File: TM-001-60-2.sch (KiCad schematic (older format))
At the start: 14 parts

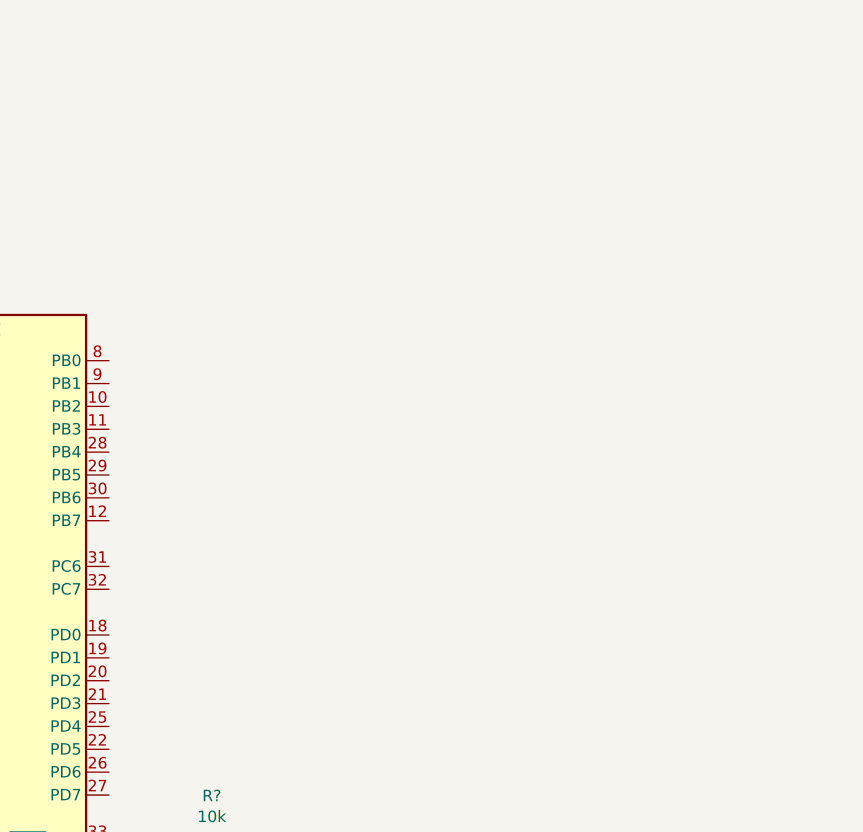
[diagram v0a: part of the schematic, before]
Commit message: Complete rest of schematic
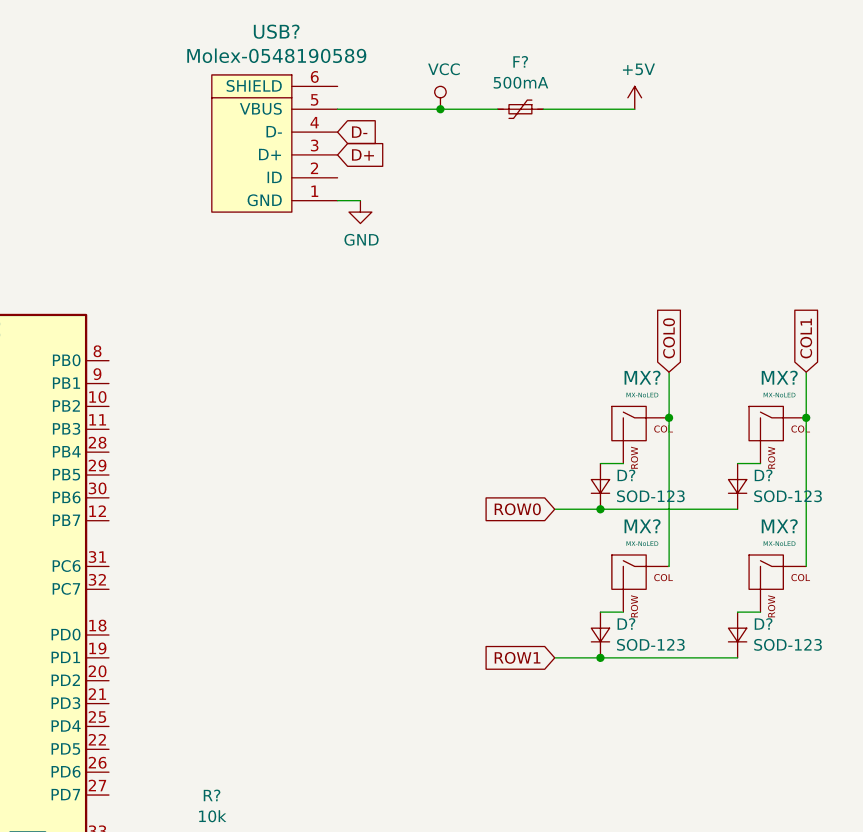
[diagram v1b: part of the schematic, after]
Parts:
- added D? (x4): SOD-123, symbol Device:D_Small
- added F?: 500mA, symbol Device:Polyfuse_Small
- added MX? (x4): MX-NoLED, symbol MX_Alps_Hybrid:MX-NoLED
- added USB?: Molex-0548190589, symbol random-keyboard-parts:Molex-0548190589
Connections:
- net +5V: now also F?.1
- net D+: now also USB?.3 (D+)
- net D-: now also USB?.4 (D-)
- net GND: now also USB?.1 (GND)
- new net: D?.2 (A), MX?.2 (ROW) (x4)
- new net COL0: MX?.1 (COL), MX?.1 (COL)
- new net COL1: MX?.1 (COL), MX?.1 (COL)
- new net ROW0: D?.1 (K), D?.1 (K)
- new net ROW1: D?.1 (K), D?.1 (K)
- new net VCC: F?.2, USB?.5 (VBUS)
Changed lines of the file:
@@
 EESchema Schematic File Version 4
+LIBS:TM-001-60-2-cache
 EELAYER 30 0
 EELAYER END
@@
 Text GLabel 1500 3600 0    50   Input ~ 0
 D-
+$Comp
+L Device:Polyfuse_Small F?
+U 1 1 6201AF9A
+P 6050 1400
+F 0 "F?" V 5845 1400 50  0000 C CNN
+F 1 "500mA" V 5936 1400 50  0000 C CNN
+F 2 "" H 6100 1200 50  0001 L CNN
+F 3 "~" H 6050 1400 50  0001 C CNN
+	1    6050 1400
+	0    1    1    0
+$EndComp
+$Comp
+L random-keyboard-parts:Molex-0548190589 USB?
+U 1 1 62018580
+P 4950 1600
+F 0 "USB?" V 5487 1567 60  0000 C CNN
+F 1 "Molex-0548190589" V 5381 1567 60  0000 C CNN
+F 2 "" H 4950 1600 60  0001 C CNN
+F 3 "" H 4950 1600 60  0001 C CNN
+	1    4950 1600
+	0    -1   -1   0
+$EndComp
+$Comp
+L power:VCC #PWR?
+U 1 1 6201E04C
+P 5700 1400
+F 0 "#PWR?" H 5700 1250 50  0001 C CNN
+F 1 "VCC" H 5717 1573 50  0000 C CNN
+F 2 "" H 5700 1400 50  0001 C CNN
+F 3 "" H 5700 1400 50  0001 C CNN
+	1    5700 1400
+	1    0    0    -1
+$EndComp
+Wire Wire Line
+	5250 1400 5700 1400
+Wire Wire Line
+	5950 1400 5700 1400
+Connection ~ 5700 1400
+$Comp
+L power:+5V #PWR?
+U 1 1 62020679
+P 6550 1400
+F 0 "#PWR?" H 6550 1250 50  0001 C CNN
+F 1 "+5V" H 6565 1573 50  0000 C CNN
+F 2 "" H 6550 1400 50  0001 C CNN
+F 3 "" H 6550 1400 50  0001 C CNN
+	1    6550 1400
+	1    0    0    -1
+$EndComp
+Wire Wire Line
+	6150 1400 6550 1400
+Text GLabel 5250 1500 2    50   Input ~ 0
+D-
+Text GLabel 5250 1600 2    50   Input ~ 0
+D+
+$Comp
+L power:GND #PWR?
+U 1 1 62022B0D
+P 5350 1800
+F 0 "#PWR?" H 5350 1550 50  0001 C CNN
+F 1 "GND" H 5355 1627 50  0000 C CNN
+F 2 "" H 5350 1800 50  0001 C CNN
+F 3 "" H 5350 1800 50  0001 C CNN
+	1    5350 1800
+	1    0    0    -1
+$EndComp
+Wire Wire Line
+	5250 1800 5350 1800
+$Comp
+L MX_Alps_Hybrid:MX-NoLED MX?
+U 1 1 62024221
+P 6550 2800
+F 0 "MX?" H 6583 3023 60  0000 C CNN
+F 1 "MX-NoLED" H 6583 2949 20  0000 C CNN
+F 2 "" H 5925 2775 60  0001 C CNN
+F 3 "" H 5925 2775 60  0001 C CNN
+	1    6550 2800
+	1    0    0    -1
+$EndComp
+$Comp
+L Device:D_Small D?
+U 1 1 62024CA8
+P 6400 3050
+F 0 "D?" V 6446 2982 50  0000 R CNN
+F 1 "SOD-123" V 6355 2982 50  0000 R CNN
+F 2 "" V 6400 3050 50  0001 C CNN
+F 3 "~" V 6400 3050 50  0001 C CNN
+	1    6400 3050
+	0    -1   -1   0
+$EndComp
+Wire Wire Line
+	6400 2950 6500 2950
+$Comp
+L MX_Alps_Hybrid:MX-NoLED MX?
+U 1 1 6202664B
+P 7150 2800
+F 0 "MX?" H 7183 3023 60  0000 C CNN
+F 1 "MX-NoLED" H 7183 2949 20  0000 C CNN
+F 2 "" H 6525 2775 60  0001 C CNN
+F 3 "" H 6525 2775 60  0001 C CNN
+	1    7150 2800
+	1    0    0    -1
+$EndComp
+$Comp
+L Device:D_Small D?
+U 1 1 62027277
+P 7000 3050
+F 0 "D?" V 7046 2982 50  0000 R CNN
+F 1 "SOD-123" V 6955 2982 50  0000 R CNN
+F 2 "" V 7000 3050 50  0001 C CNN
+F 3 "~" V 7000 3050 50  0001 C CNN
+	1    7000 3050
+	0    -1   -1   0
+$EndComp
+Wire Wire Line
+	7000 2950 7100 2950
+$Comp
+L MX_Alps_Hybrid:MX-NoLED MX?
+U 1 1 6202C76A
+P 6550 3450
+F 0 "MX?" H 6583 3673 60  0000 C CNN
+F 1 "MX-NoLED" H 6583 3599 20  0000 C CNN
+F 2 "" H 5925 3425 60  0001 C CNN
+F 3 "" H 5925 3425 60  0001 C CNN
+	1    6550 3450
+	1    0    0    -1
+$EndComp
+$Comp
+L Device:D_Small D?
+U 1 1 6202CF72
+P 6400 3700
+F 0 "D?" V 6446 3632 50  0000 R CNN
+F 1 "SOD-123" V 6355 3632 50  0000 R CNN
+F 2 "" V 6400 3700 50  0001 C CNN
+F 3 "~" V 6400 3700 50  0001 C CNN
+	1    6400 3700
+	0    -1   -1   0
+$EndComp
+Wire Wire Line
+	6400 3600 6500 3600
+$Comp
+L MX_Alps_Hybrid:MX-NoLED MX?
+U 1 1 6202E4F6
+P 7150 3450
+F 0 "MX?" H 7183 3673 60  0000 C CNN
+F 1 "MX-NoLED" H 7183 3599 20  0000 C CNN
+F 2 "" H 6525 3425 60  0001 C CNN
+F 3 "" H 6525 3425 60  0001 C CNN
+	1    7150 3450
+	1    0    0    -1
+$EndComp
+$Comp
+L Device:D_Small D?
+U 1 1 6202F015
+P 7000 3700
+F 0 "D?" V 7046 3632 50  0000 R CNN
+F 1 "SOD-123" V 6955 3632 50  0000 R CNN
+F 2 "" V 7000 3700 50  0001 C CNN
+F 3 "~" V 7000 3700 50  0001 C CNN
+	1    7000 3700
+	0    -1   -1   0
+$EndComp
+Wire Wire Line
+	7000 3600 7100 3600
+Wire Wire Line
+	6700 3400 6700 2750
+Connection ~ 6700 2750
+Wire Wire Line
+	6700 2750 6700 2550
+Wire Wire Line
+	7300 3400 7300 2750
+Connection ~ 7300 2750
+Wire Wire Line
+	7300 2750 7300 2550
+Wire Wire Line
+	7000 3150 6400 3150
+Connection ~ 6400 3150
+Wire Wire Line
+	6400 3150 6200 3150
+Wire Wire Line
+	7000 3800 6400 3800
+Connection ~ 6400 3800
+Wire Wire Line
+	6400 3800 6200 3800
+Text GLabel 6200 3150 0    50   Input ~ 0
+ROW0
+Text GLabel 6200 3800 0    50   Input ~ 0
+ROW1
+Text GLabel 6700 2550 1    50   Input ~ 0
+COL0
+Text GLabel 7300 2550 1    50   Input ~ 0
+COL1
 $EndSCHEMATC

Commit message: ready to create pcb
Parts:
- C1, C2, C3, C4, C5, C6, C7: renamed from C?; footprint (none) -> Capacitor_SMD:C_0805_2012Metric
- D1, D2, D3, D4: renamed from D?; footprint (none) -> Diode_SMD:D_SOD-123
- F1: renamed from F?; footprint (none) -> Fuse:Fuse_1206_3216Metric
- MX1, MX2, MX3, MX4: renamed from MX?; footprint (none) -> MX_Alps_Hybrid:MX-1U-NoLED
- SW1: renamed from SW?; footprint (none) -> random-keyboard-parts:SKQG-1155865
- USB1: renamed from USB?; footprint (none) -> random-keyboard-parts:Molex-0548190589
- Y1: renamed from Y?; footprint (none) -> Crystal:Crystal_SMD_3225-4Pin_3.2x2.5mm
- gave numbers to parts that had none: 5

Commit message: fixed footprint assigning
i forgor resistors
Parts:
- R1, R2, R3, R4: footprint (none) -> Resistor_SMD:R_0805_2012Metric
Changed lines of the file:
@@
 F 0 "R4" V 4504 4600 50  0000 C CNN
 F 1 "10k" V 4595 4600 50  0000 C CNN
-F 2 "" H 4700 4600 50  0001 C CNN
+F 2 "Resistor_SMD:R_0805_2012Metric" H 4700 4600 50  0001 C CNN
 F 3 "~" H 4700 4600 50  0001 C CNN
 	1    4700 4600
@@
 F 0 "R2" V 2104 3500 50  0000 C CNN
 F 1 "22" V 2195 3500 50  0000 C CNN
-F 2 "" H 2300 3500 50  0001 C CNN
+F 2 "Resistor_SMD:R_0805_2012Metric" H 2300 3500 50  0001 C CNN
 F 3 "~" H 2300 3500 50  0001 C CNN
 	1    2300 3500
@@
 F 0 "R3" V 1604 3600 50  0000 C CNN
 F 1 "22" V 1695 3600 50  0000 C CNN
-F 2 "" H 1800 3600 50  0001 C CNN
+F 2 "Resistor_SMD:R_0805_2012Metric" H 1800 3600 50  0001 C CNN
 F 3 "~" H 1800 3600 50  0001 C CNN
 	1    1800 3600
@@
 F 0 "R1" H 3059 2196 50  0000 L CNN
 F 1 "10k" H 3059 2105 50  0000 L CNN
-F 2 "" H 3000 2150 50  0001 C CNN
+F 2 "Resistor_SMD:R_0805_2012Metric" H 3000 2150 50  0001 C CNN
 F 3 "~" H 3000 2150 50  0001 C CNN
 	1    3000 2150

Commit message: saved schematic
i forgor *insert skull emoji*
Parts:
- MX1, MX2, MX3, MX4: footprint MX_Alps_Hybrid:MX-1U-NoLED -> MX_Alps_Hybrid:MX-1U
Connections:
- net COL0: now also U1.29 (PB5)
- net COL1: now also U1.28 (PB4)
- net ROW0: now also U1.27 (PD7)
- net ROW1: now also U1.30 (PB6)
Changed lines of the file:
@@
 F 0 "MX1" H 6583 3023 60  0000 C CNN
 F 1 "MX-NoLED" H 6583 2949 20  0000 C CNN
-F 2 "MX_Alps_Hybrid:MX-1U-NoLED" H 5925 2775 60  0001 C CNN
+F 2 "MX_Alps_Hybrid:MX-1U" H 5925 2775 60  0001 C CNN
 F 3 "" H 5925 2775 60  0001 C CNN
 	1    6550 2800
@@
 F 0 "MX2" H 7183 3023 60  0000 C CNN
 F 1 "MX-NoLED" H 7183 2949 20  0000 C CNN
-F 2 "MX_Alps_Hybrid:MX-1U-NoLED" H 6525 2775 60  0001 C CNN
+F 2 "MX_Alps_Hybrid:MX-1U" H 6525 2775 60  0001 C CNN
 F 3 "" H 6525 2775 60  0001 C CNN
 	1    7150 2800
@@
 F 0 "MX3" H 6583 3673 60  0000 C CNN
 F 1 "MX-NoLED" H 6583 3599 20  0000 C CNN
-F 2 "MX_Alps_Hybrid:MX-1U-NoLED" H 5925 3425 60  0001 C CNN
+F 2 "MX_Alps_Hybrid:MX-1U" H 5925 3425 60  0001 C CNN
 F 3 "" H 5925 3425 60  0001 C CNN
 	1    6550 3450
@@
 F 0 "MX4" H 7183 3673 60  0000 C CNN
 F 1 "MX-NoLED" H 7183 3599 20  0000 C CNN
-F 2 "MX_Alps_Hybrid:MX-1U-NoLED" H 6525 3425 60  0001 C CNN
+F 2 "MX_Alps_Hybrid:MX-1U" H 6525 3425 60  0001 C CNN
 F 3 "" H 6525 3425 60  0001 C CNN
 	1    7150 3450
@@
 Text GLabel 7300 2550 1    50   Input ~ 0
 COL1
+Text GLabel 4250 2900 2    50   Input ~ 0
+COL1
+Text GLabel 4250 3000 2    50   Input ~ 0
+COL0
+Text GLabel 4250 3100 2    50   Input ~ 0
+ROW1
+Text GLabel 4250 4400 2    50   Input ~ 0
+ROW0
 $EndSCHEMATC
